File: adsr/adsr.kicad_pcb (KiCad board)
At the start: 2 copper layers, 69.2 x 71.1 mm, 57 parts, among them J1 Trigger, J2 Gate, J3 OUT, J4 Conn_02x05_Odd_Even, SW1 SW_Push, SW2 SW_SPDT, U1 4066, U2 TL082, U3 40106, U4 TL084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

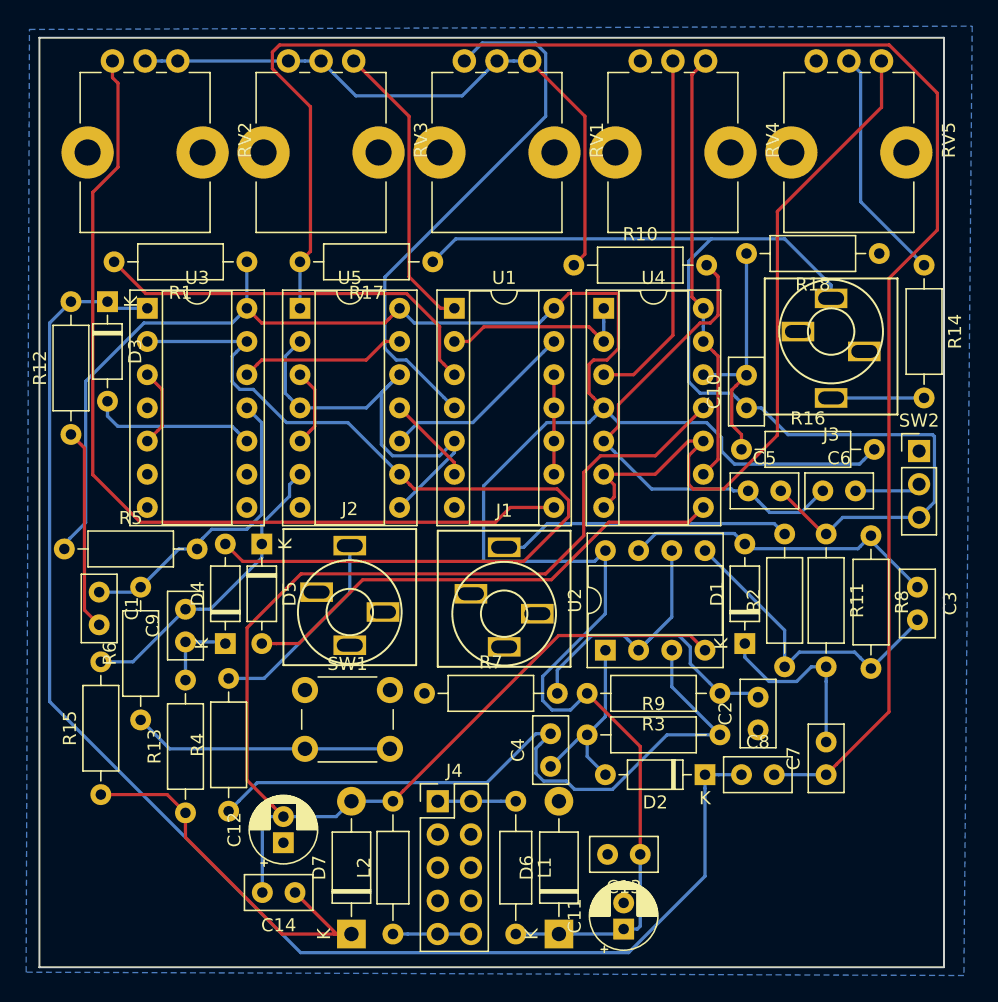
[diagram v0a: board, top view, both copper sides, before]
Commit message: Modified the eurorackpin schematic and cleaned up
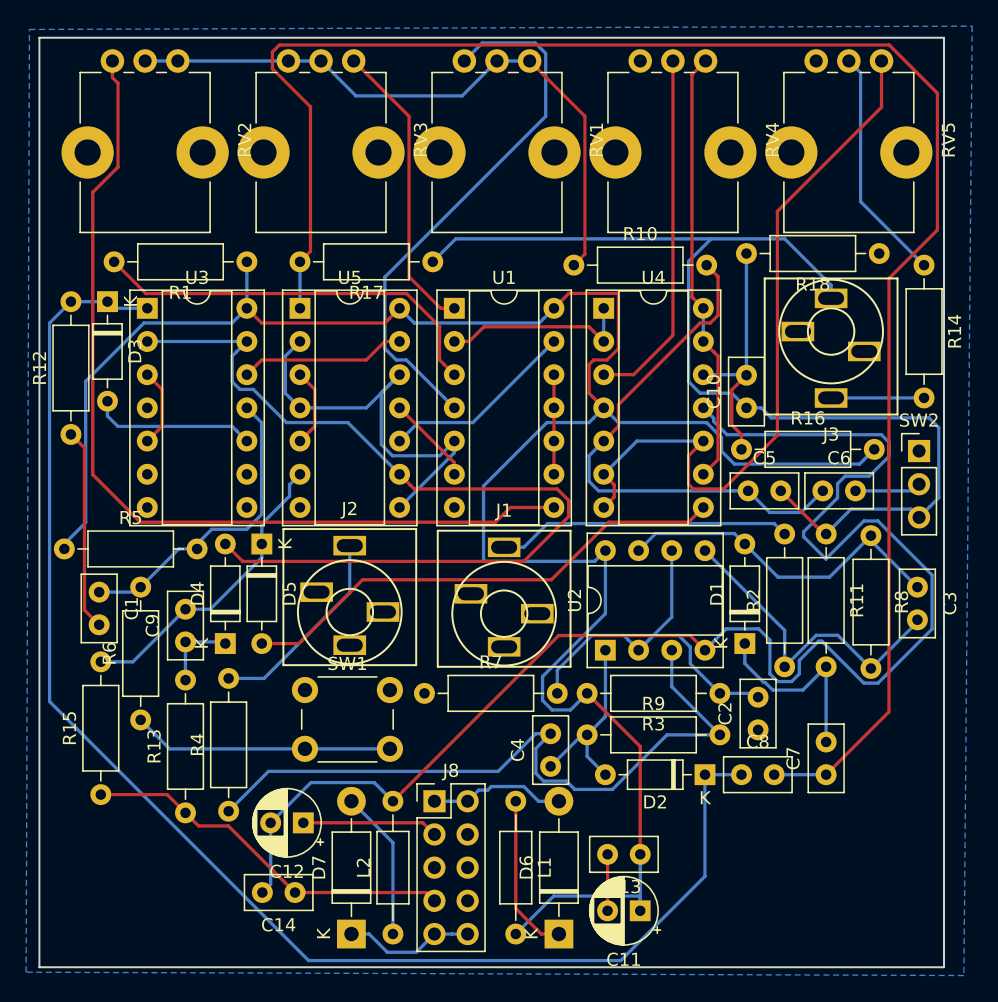
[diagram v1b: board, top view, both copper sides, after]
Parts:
- removed J4: Conn_02x05_Odd_Even, Connector_PinHeader_2.54mm:PinHeader_2x05_P2.54mm_Vertical
- added J8: Conn_02x05_Odd_Even, Connector_PinHeader_2.54mm:PinHeader_2x05_P2.54mm_Vertical, F.Cu at (62.0, 80.0)
- C11, C12: footprint Capacitor_THT:CP_Radial_D5.0mm_P2.00mm -> Capacitor_THT:CP_Radial_D5.0mm_P2.50mm
- moved C12 2.16 mm to (51.9, 81.7), turned to 180 degrees
- moved C11 1.89 mm to (77.7, 88.4), turned to 180 degrees
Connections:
- D6 pad 1: 12V -> /EURORACKPIN/12Vto5V
- D6 pad 2: GND -> 12VC
- D7 pad 1: GND -> -12VC
- D7 pad 2: -12V -> Net-(D7-Pad2)
- L1 pad 1: 12VC -> /EURORACKPIN/12Vto5V
- L2 pad 1: -12VC -> Net-(D7-Pad2)
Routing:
- net GND: track 144.5 -> 159.1 mm
- net /EURORACKPIN/12Vto5V: track 0.00 -> 12.3 mm
- net Net-(D7-Pad2): track 0.00 -> 11.5 mm
- net -12V: track 105.9 -> 116.6 mm
- net 12VC: track 5.97 -> 10.5 mm
- net -12VC: track 5.97 -> 10.0 mm
- net Net-(C5-Pad1): track 37.6 -> 41.0 mm
- net Net-(C3-Pad1): track 24.6 -> 26.4 mm
- net Net-(C3-Pad2): track 24.2 -> 25.3 mm
- net 12V: track 170.9 -> 171.8 mm
- net Net-(C7-Pad2): track 14.3 -> 15.1 mm
- net Man-Gate: track 108.4 -> 108.9 mm
